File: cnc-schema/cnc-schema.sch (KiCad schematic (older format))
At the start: 24 parts, among them P1 STEPPER-X, P10 Connector P3, P11 Connector P4, P2 STEPPER-Y, P3 STEPPER-Z, P4 STEPPER-X, P5 STEPPER-Y, P6 STEPPER-Z, P7 on/off sw, P8 Connector P1, P9 Connector P2, U1 HWS1000-48, U2 KS400A-230S24-SCN, U3 P5V1A, U4 LoDroUp

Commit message: updated schema
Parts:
- added F1: 5A, symbol Fuse
- added F2: 15A, symbol Fuse
- added F3: 10A, symbol Fuse
- added F4: 2A, symbol Fuse
- added R1: 1k, symbol R
- added RL1: 230V 20A, symbol FINDER-44.62
- added SW1: MAIN_PWR_SWITCH, symbol SW_DPST_x2
- added SW2: PC_PWR_SWITCH, symbol SW_DPST_x2
- added SW3: DRIVER_PWR_SWITCH, symbol SW_DPST_x2
- added SW4: DRIVER_ENABLE_SWITCH, symbol SW_DPST_x2
- added SW5: SPINDLE_PWR_SWITCH, symbol SW_DPST_x2
- P1, P4: value STEPPER-X -> STEPPER_X
- P10: value Connector P3 -> OUT1 P3
- P11: value Connector P4 -> OUT2 P4
- P2, P5: value STEPPER-Y -> STEPPER_Y
- P3, P6: value STEPPER-Z -> STEPPER_Z
- P7: value on/off sw -> BBB_POWER
- P8: value Connector P1 -> IN1 P1
- P9: value Connector P2 -> IN2 P2
- U3: value P5V1A -> OFM-0101; symbol P5V1A -> OFM-0101
- U4: value LoDroUp -> N9510; symbol LoDroUp -> N9510
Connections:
- net labels added: AGND, AIN0, AIN1, AIN2, AIN3, AVDD, A_DIR, A_STEP, DRIVER_ENABLE_SWITCH, Earth, IN11, IN12, IN13, IN14, IN15, IN16, L, L_IN, N, N_IN, OUT1, OUT2, OUT3, OUT4, OUT5, OUT6, X1, X2, X3, X4, Y1, Y2, Y3, Y4, Z1, Z2, Z3, Z4, Z_PROBE
- wire segments 96 -> 144
- no-connect marks 0 -> 39
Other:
- note added: "=BLK"
- note added: "=BLU"
- note added: "=GRN"
- note added: "=ORG"
- note added: "=PRPL"
- note added: "=RED"
- note added: "=YEL"
- note added: "BeagleBone Black & Panther Cape"
- note added: "StepSyn 1.8 DEG\n103H7126-07G3"
- note added: "Vexta 1.8 DEG\nC8124-9212H"
- moved on the sheet: L1, L2, L3, L4, L5, L6, P1, P10, P11, P2, P3, P4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

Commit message: finalized schema
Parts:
- added P12: BRUSHLESS_HALL, symbol CONN_01X05
- added P13: BRUSHLESS_UVW, symbol CONN_01X03
- added R2, R4: 10k, symbol R
- added R3: 20k, symbol R
- added RV1: 10K, symbol POT
- added SW6: EMERGENCY_STOP_SWITCH, symbol SW_DPST_x2
- added SW7: Z_PROBE_LIMIT_SWITCH, symbol SW_DPST_x2
- added SW8: SPINDLE_ENABLE, symbol SW_DPST_x2
- added SW9: SPINDLE_DIR_SWITCH, symbol SW_DPDT_x2
- added U10, U11, U12, U13, U6, U7, U8, U9: Lj12a3-4-z/Ax, symbol Lj12a3-4-z/Ax
- added U5: JYQD_V7.3Ei, symbol JYQD_V7.3Ei
- F3: value 10A -> 2A
- F4: value 2A -> 10A
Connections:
- net labels added: GNDPWR, SPINDLE_RPM
- net labels removed: Earth, IN11, L_IN, N_IN
- wire segments 144 -> 211
- no-connect marks 39 -> 38
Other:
- note added: "230VAC"
- note added: "Limit Sensors"
- note added: "Power Supplys"
- note added: "Spindle Motor Driver"
- note added: "Stepper"
- note added: "Stepper Drivers"
- note added: "Unconnected Nets"
- moved on the sheet: P10, P11, P4, P5, P6, P7, P8, P9, R1, SW1A, SW2A, SW4A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

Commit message: refined schema
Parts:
- added L7, L8, L9: L, symbol L
- added P14: SPINDLE_MOTOR, symbol CONN_01X03
- added P15: SPINDLE_HALL, symbol CONN_01X05
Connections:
- net labels added: AGND0, AGND1, AVDD0, AVDD1
- net labels removed: AGND, AVDD
- wire segments 211 -> 337
- no-connect marks 38 -> 47
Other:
- note added: "1"
- note added: "2"
- note added: "3"
- note added: "5V = GRY"
- note added: "CNC Switches"
- note added: "GND = YEL"
- note added: "Ha = GRN"
- note added: "Hb = BRN"
- note added: "Hc = WHT"
- note added: "Maxxon 136210\n24V, 12.5A, 250W, 8670rpm, 311mNm"
- note added: "Unconnected Cape Pins"
- note removed: "Unconnected Nets"
- moved on the sheet: F2, F3, F4, L3, L4, L5, L6, P10, P11, P12, P13, P2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

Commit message: minor schema changes
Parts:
- P12: value BRUSHLESS_HALL -> SPINDLE_HALL
- P13: value BRUSHLESS_UVW -> SPINDLE_UVW
- P14: value SPINDLE_MOTOR -> SPINDLE_UVW
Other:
- note added: "StepSyn 1.8 DEG 3.5A\n103H7126-07G3"
- note added: "Vexta 1.8 DEG 3.75A\nC8124-9212H"
- note removed: "StepSyn 1.8 DEG\n103H7126-07G3"
- note removed: "Vexta 1.8 DEG\nC8124-9212H"
- moved on the sheet: F2, F4, P4, P5, P6, R1, SW3A, SW4A, SW5A, U1, U2, UX1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

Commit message: minor schema changes
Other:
- note added: "Maxxon 136210 24V,\n12.5A, 250W, 8670rpm,\n311mNm"
- note removed: "Maxxon 136210\n24V, 12.5A, 250W, 8670rpm, 311mNm"
- moved on the sheet: F1, F3, L1, L2, L3, L4, L5, L6, L7, L8, L9, P1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

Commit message: minor schema changes
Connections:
- net GND: now also U2.X2.3 (OUT-), U2.X2.4 (OUT-)
- net at F4.1, U2.X2.1 (27V_OUT+): now also U2.X2.2 (27V_OUT+)
- net at U2.X4.2 (+COntrol): now also SW5.1 (A)
- net at U2.X5.1 (Feedback): now also SW5.2 (B)
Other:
- note added: "X/Y/Z-Axis Stepper"
- note removed: "Stepper"
- moved on the sheet: F1, F2, F3, F4, L1, L2, L5, L6, L7, L8, L9, P1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

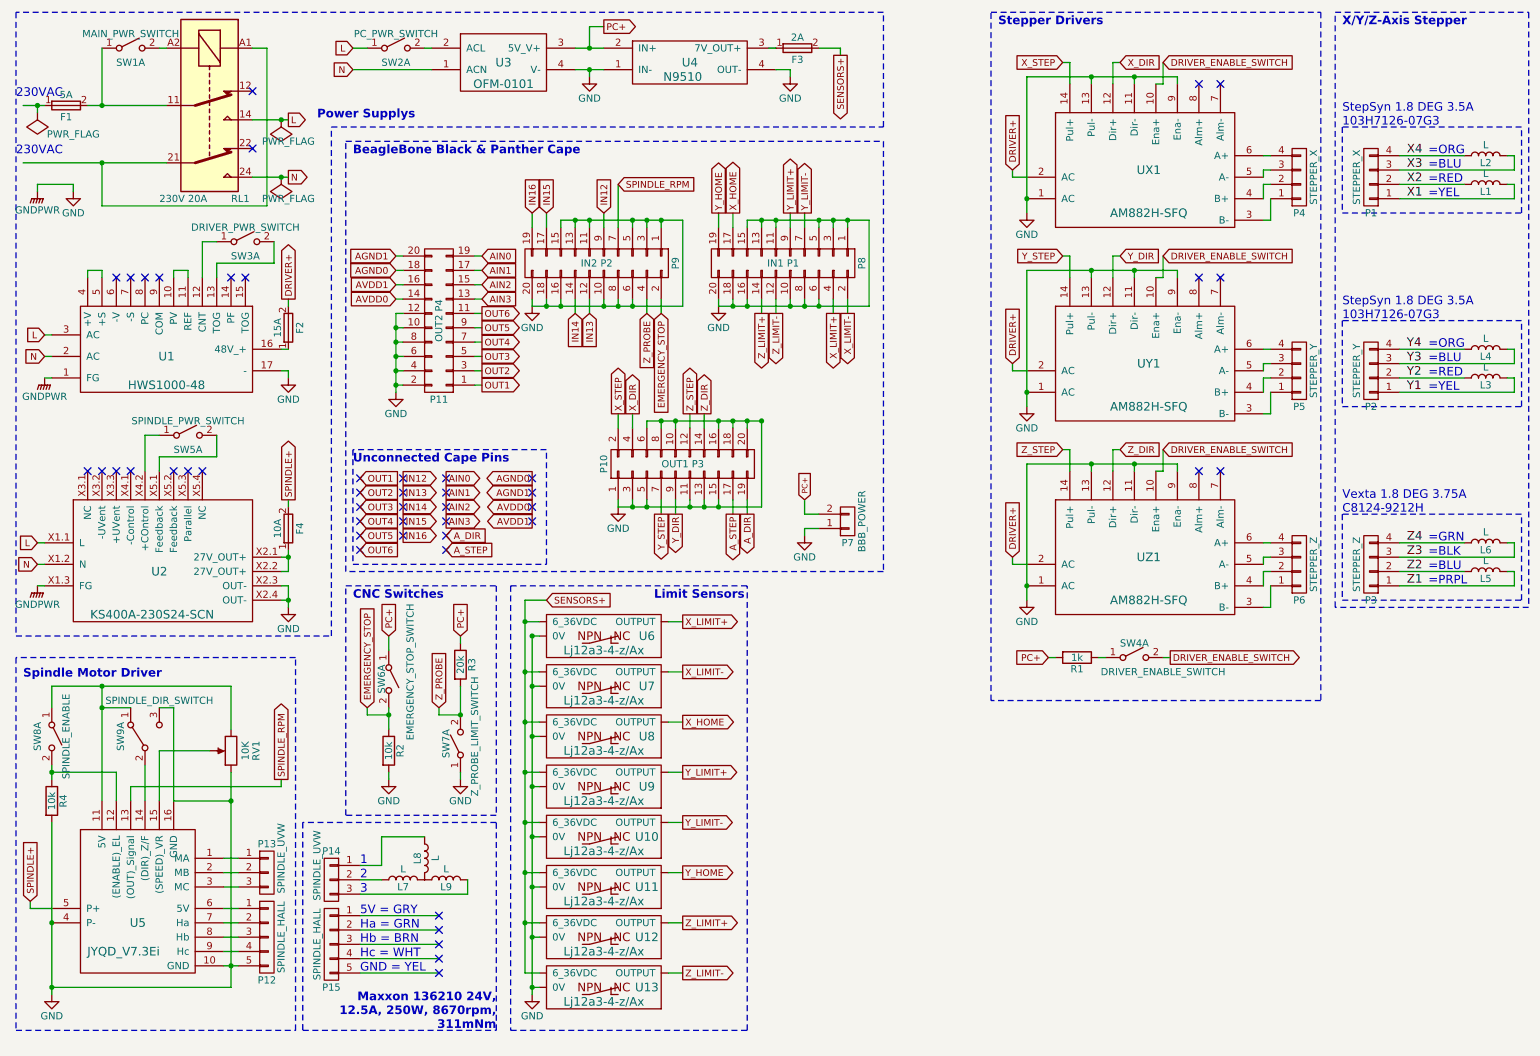
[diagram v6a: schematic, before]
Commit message: corrected many labels, removed and driectly connected switches to panther conn.
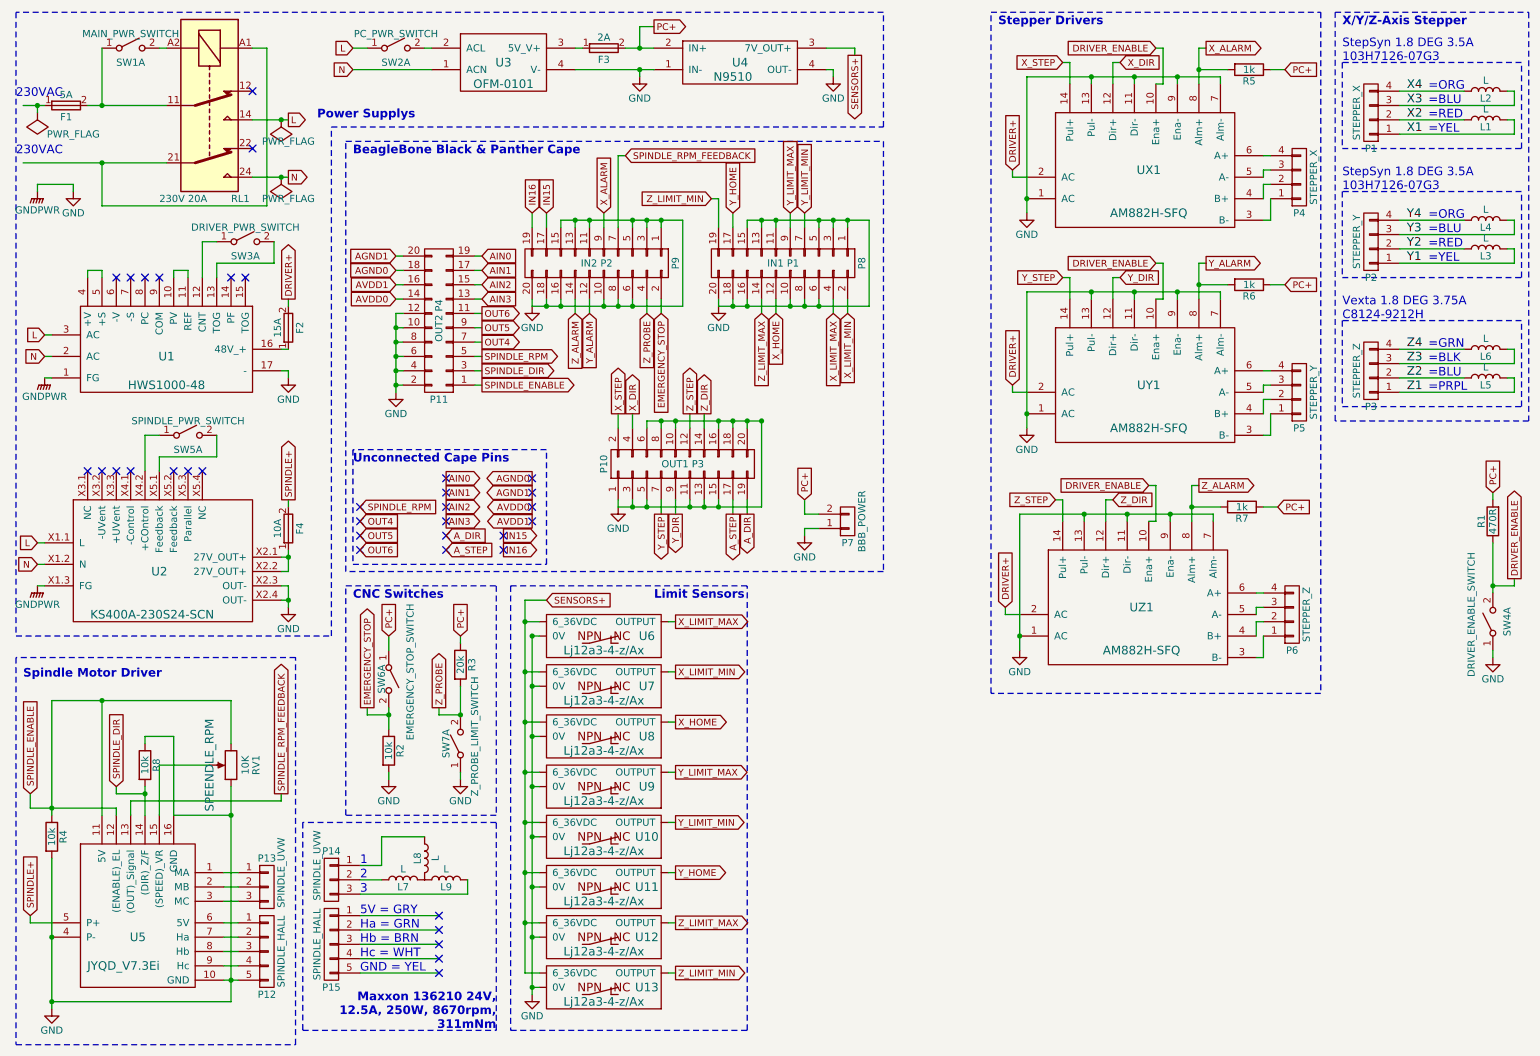
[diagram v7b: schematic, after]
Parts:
- removed SW8: SPINDLE_ENABLE, symbol SW_DPST_x2
- removed SW9: SPINDLE_DIR_SWITCH, symbol SW_DPDT_x2
- added R5, R6, R7: 1k, symbol R
- added R8: 10k, symbol R
- R1: value 1k -> 470R
- RV1: DESC (none) -> SPEENDLE_RPM
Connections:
- net DRIVER_ENABLE_SWITCH is gone; now on net DRIVER_ENABLE: SW4.2 (B), UX1.10 (Ena+), UY1.10 (Ena+), UZ1.10 (Ena+)
- net IN12 is gone; now on net X_ALARM: P9.9 (P9)
- net IN13 is gone; now on net Y_ALARM: P9.12 (P12)
- net IN14 is gone; now on net Z_ALARM: P9.14 (P14)
- net OUT1 is gone; now on net SPINDLE_ENABLE: P11.1 (P1)
- net OUT2 is gone; now on net SPINDLE_DIR: P11.3 (P3)
- net OUT3 is gone; now on net SPINDLE_RPM: P11.5 (P5)
- net X_LIMIT+ is gone; now on net X_LIMIT_MAX: P8.4 (P4), U6.~
- net X_LIMIT- is gone; now on net X_LIMIT_MIN: P8.2 (P2), U7.~
- net Y_LIMIT+ is gone; now on net Y_LIMIT_MAX: P8.9 (P9), U9.~
- net Y_LIMIT- is gone; now on net Y_LIMIT_MIN: P8.7 (P7), U10.~
- net Z_LIMIT+ is gone; now on net Z_LIMIT_MAX: P8.14 (P14), U12.~
- net GND: now also SW4.1 (A), UX1.7 (Alm-), UY1.7 (Alm-), UZ1.7 (Alm-), R8.1
- net PC+: now also F3.2, R5.1, R6.1, R7.1; no longer U3.3 (5V_V+)
- net SENSORS+: now also U4.3 (7V_OUT+); no longer F3.2
- net SPINDLE_RPM: no longer P9.7 (P7), U5.13 ((OUT)_Signal)
- net X_HOME: now also P8.12 (P12); no longer P8.17 (P17)
- net Y_HOME: now also P8.17 (P17); no longer P8.19 (P19)
- net X_ALARM: now reaches UX1.8 (Alm+)
- net X_ALARM: now also R5.2
- net Y_ALARM: now reaches UY1.8 (Alm+)
- net Y_ALARM: now also R6.2
- net Z_ALARM: now reaches UZ1.8 (Alm+)
- net Z_ALARM: now also R7.2
- net at F3.1: now also U3.3 (5V_V+); no longer U4.3 (7V_OUT+)
- net SPINDLE_ENABLE: now reaches RV1.3, U5.11 (5V)
- net SPINDLE_ENABLE: now also R4.1, U5.12 ((ENABLE)_EL)
- net SPINDLE_DIR: now reaches U5.14 ((DIR)_Z/F)
- net SPINDLE_DIR: now also R8.2
- net DRIVER_ENABLE: now reaches R1.1
- net DRIVER_ENABLE: no longer SW4.1 (A)
- net X_LIMIT_MAX: now reaches U6.~
- net X_LIMIT_MIN: now reaches U7.~
- net Y_LIMIT_MAX: now reaches U9.~
- net Y_LIMIT_MIN: now reaches U10.~
- net Z_LIMIT_MAX: now reaches U12.~
- net Z_LIMIT_MIN: now reaches U13.~
- net Z_LIMIT_MIN: now also P8.19 (P19)
- removed net Z_LIMIT-: P8.12 (P12), U13.~
- new net SPINDLE_RPM_FEEDBACK: P9.7 (P7), U5.13 ((OUT)_Signal)
- no-connect marks 47 -> 36
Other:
- moved on the sheet: F3, L1, L2, L3, L4, L5, L6, P1, P12, P13, P2, P3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

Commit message: minor chagnes
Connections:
- net GND: now also U2.X4.1 (-Control)
- net PC+: now also SW5.1 (A)
- net at U2.X4.2 (+COntrol): now also SW5.2 (B); no longer SW5.1 (A)
- net at U2.X5.1 (Feedback): no longer SW5.2 (B)
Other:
- moved on the sheet: F4, SW5A
